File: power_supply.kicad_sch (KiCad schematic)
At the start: 10 parts, among them J1 USB4110-GF-A, U2 MIC5317-3.3YMT-TZ, U3 ACZRC5340B-G, U5 LMC7660IMX/NOPB

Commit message: Almost done. Just going to try and change something
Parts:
- removed U2: MIC5317-3.3YMT-TZ, DFN4_1X1_MCH, symbol CMPE2750:MIC5317-3.3YMT-TZ
- added U2: LP5907SNX-3.3/NOPB, DQN0004A, symbol CMPE2750:LP5907SNX-3.3_NOPB
- J1: value USB4110-GF-A -> USB4510-03-1-A; footprint USB4110-GF-A_GCT -> USB4510-03-1-A_GCT; symbol CMPE2750:USB4110-GF-A -> CMPE2750:USB4510-03-1-A
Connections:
- net GND: now also J1.B1-A12 (GND), U2.2 (GND), U2.5 (EP); no longer J1.A12-B1 (GND)
- net VBUS: now also J1.B4-A9 (VBUS), U2.3 (EN), U2.4 (VIN); no longer J1.A9-B4 (VBUS)
- net VDD: now also U2.1 (VOUT)
- no-connect marks 3 -> 5
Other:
- moved on the sheet: C1, C2, U3

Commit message: Schematic is done?
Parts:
- removed C1, C2: 1µF, LMK212G_TAY, symbol CMPE2750:LMK212B7105KGHTR
- removed U3: ACZRC5340B-G, ACZRC-G, symbol CMPE2750:ACZRC5340B-G
- added C1: 10µF, Capacitor_SMD:C_1206_3216Metric, symbol CMPE2750:CL31A106KOHNNNE
- added C2: 1µF, Capacitor_SMD:C_1206_3216Metric, symbol CMPE2750:CL31A106KOHNNNE
- added D1, D32: 5.6V~6V, Diode_SMD:D_SOD-123, symbol Device:D_Zener
- C3, C4: footprint CAP_CL31_SAM -> Capacitor_SMD:C_1206_3216Metric
- R1, R2: footprint RC0603N_YAG -> Resistor_SMD:R_0603_1608Metric
- U5: footprint M08A_TEX -> Package_SO:SOIC-8_3.9x4.9mm_P1.27mm
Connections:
- net -5V: now also D32.2 (A)
- net GND: now also C1.2, C2.2, D1.2 (A), D32.1 (K)
- net VBUS: now also C1.1, D1.1 (K)
- net VDD: now also C2.1

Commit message: Added mounting holes to the schematic, reset the annotations, updated a few footprints, and fixed some issues that were discovered on the ERC.
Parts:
- J6: renamed from J1; footprint USB4510-03-1-A_GCT -> CMPE2750:USB4510-03-1-A_GCT
- U2: footprint DQN0004A -> CMPE2750:DQN0004A
- renumbered C1 to C10, C2 to C11, C3 to C12, C4 to C13, D32 to D2, R1 to R29, R2 to R30, U5 to U3
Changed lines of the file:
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@@
+	)
+	(junction
+		(at 267.97 67.31)
+		(diameter 0)
+		(color 0 0 0 0)
 	)
 	(junction
@@
 	(wire
 		(pts
-			(xy 127 73.66) (xy 58.42 73.66)
-		)
-		(stroke
-			(width 0)
-			(type default)
-		)
-	)
-	(wire
-		(pts
 			(xy 59.69 137.16) (xy 58.42 137.16)
 		)
@@
 	(wire
 		(pts
+			(xy 58.42 73.66) (xy 127 73.66)
+		)
+		(stroke
+			(width 0)
+			(type default)
+		)
+	)
+	(wire
+		(pts
 			(xy 151.13 53.34) (xy 151.13 73.66)
 		)
@@
 	(wire
 		(pts
+			(xy 267.97 67.31) (xy 260.35 67.31)
+		)
+		(stroke
+			(width 0)
+			(type default)
+		)
+	)
+	(wire
+		(pts
 			(xy 119.38 152.4) (xy 119.38 153.67)
 		)
@@
 	(wire
 		(pts
-			(xy 271.78 67.31) (xy 260.35 67.31)
+			(xy 271.78 67.31) (xy 267.97 67.31)
 		)
 		(stroke
@@
 		(dnp no)
 		(fields_autoplaced yes)
-		(property "Reference" "C4"
+		(property "Reference" "C13"
 			(at 123.19 144.7799 90)
 			(effects
@@
 			(project ""
 				(path "/a86318a1-888d-4137-89a5-221e5a1bc171/0066a7d7-f2ad-4520-976c-e35e03c74cdf"
-					(reference "C4")
+					(reference "C13")
+					(unit 1)
+				)
+			)
+		)
+	)
+	(symbol
+		(lib_id "power:PWR_FLAG")
+		(at 267.97 67.31 0)
+		(unit 1)
+		(exclude_from_sim no)
+		(in_bom yes)
+		(on_board yes)
+		(dnp no)
+		(fields_autoplaced yes)
+		(property "Reference" "#FLG02"
+			(at 267.97 65.405 0)
+			(effects
+				(font
+					(size 1.27 1.27)
+				)
+				(hide yes)
+			)
+		)
+		(property "Value" "PWR_FLAG"
+			(at 267.97 62.23 0)
+			(effects
+				(font
+					(size 1.27 1.27)
+				)
+			)
+		)
+		(property "Footprint" ""
+			(at 267.97 67.31 0)
+			(effects
+				(font
+					(size 1.27 1.27)
+				)
+				(hide yes)
+			)
+		)
+		(property "Datasheet" "~"
+			(at 267.97 67.31 0)
+			(effects
+				(font
+					(size 1.27 1.27)
+				)
+				(hide yes)
+			)
+		)
+		(property "Description" "Special symbol for telling ERC where power comes from"
+			(at 267.97 67.31 0)
+			(effects
+				(font
+					(size 1.27 1.27)
+				)
+				(hide yes)
+			)
+		)
+		(pin "1"
+		)
+		(instances
+			(project ""
+				(path "/a86318a1-888d-4137-89a5-221e5a1bc171/0066a7d7-f2ad-4520-976c-e35e03c74cdf"
+					(reference "#FLG02")
 					(unit 1)
 				)
@@
 		(dnp no)
 		(fields_autoplaced yes)
-		(property "Reference" "U5"
+		(property "Reference" "U3"
 			(at 87.63 121.92 0)
 			(effects
@@
 					(italic yes)
 				)
+				(hide yes)
 			)
 		)
@@
 			(project ""
 				(path "/a86318a1-888d-4137-89a5-221e5a1bc171/0066a7d7-f2ad-4520-976c-e35e03c74cdf"
-					(reference "U5")
+					(reference "U3")
 					(unit 1)
 				)
@@
 		(dnp no)
 		(fields_autoplaced yes)
-		(property "Reference" "#PWR08"
+		(property "Reference" "#PWR050"
 			(at 119.38 160.02 0)
 			(effects
@@
 			(project ""
 				(path "/a86318a1-888d-4137-89a5-221e5a1bc171/0066a7d7-f2ad-4520-976c-e35e03c74cdf"
-					(reference "#PWR08")
+					(reference "#PWR050")
 					(unit 1)
 				)
@@
 		(dnp no)
 		(fields_autoplaced yes)
-		(property "Reference" "#PWR01"
+		(property "Reference" "#PWR044"
 			(at 58.42 83.82 0)
 			(effects
@@
 			(project ""
 				(path "/a86318a1-888d-4137-89a5-221e5a1bc171/0066a7d7-f2ad-4520-976c-e35e03c74cdf"
-					(reference "#PWR01")
+					(reference "#PWR044")
 					(unit 1)
 				)
@@
 		(dnp no)
 		(fields_autoplaced yes)
-		(property "Reference" "#PWR03"
+		(property "Reference" "#PWR045"
 			(at 198.12 88.9 0)
 			(effects
@@
 			(project ""
 				(path "/a86318a1-888d-4137-89a5-221e5a1bc171/0066a7d7-f2ad-4520-976c-e35e03c74cdf"
-					(reference "#PWR03")
+					(reference "#PWR045")
 					(unit 1)
 				)
@@
 		(dnp no)
 		(fields_autoplaced yes)
-		(property "Reference" "C2"
+		(property "Reference" "C11"
 			(at 264.16 77.4699 90)
 			(effects
@@
 			(project "CMPE2750"
 				(path "/a86318a1-888d-4137-89a5-221e5a1bc171/0066a7d7-f2ad-4520-976c-e35e03c74cdf"
-					(reference "C2")
+					(reference "C11")
 					(unit 1)
 				)
@@
 		(dnp no)
 		(fields_autoplaced yes)
-		(property "Reference" "#PWR07"
+		(property "Reference" "#PWR049"
 			(at 58.42 149.86 0)
 			(effects
@@
 			(project ""
 				(path "/a86318a1-888d-4137-89a5-221e5a1bc171/0066a7d7-f2ad-4520-976c-e35e03c74cdf"
-					(reference "#PWR07")
+					(reference "#PWR049")
 					(unit 1)
 				)
@@
 		(dnp no)
 		(fields_autoplaced yes)
-		(property "Reference" "#PWR05"
+		(property "Reference" "#PWR043"
 			(at 209.55 64.77 0)
 			(effects
@@
 			(project ""
 				(path "/a86318a1-888d-4137-89a5-221e5a1bc171/0066a7d7-f2ad-4520-976c-e35e03c74cdf"
-					(reference "#PWR05")
+					(reference "#PWR043")
 					(unit 1)
 				)
@@
 		(dnp no)
 		(fields_autoplaced yes)
-		(property "Reference" "J1"
+		(property "Reference" "J6"
 			(at 104.14 35.56 0)
 			(effects
@@
 			)
 		)
-		(property "Footprint" "USB4510-03-1-A_GCT"
+		(property "Footprint" "CMPE2750:USB4510-03-1-A_GCT"
 			(at 83.82 45.72 0)
 			(effects
@@
 			(project ""
 				(path "/a86318a1-888d-4137-89a5-221e5a1bc171/0066a7d7-f2ad-4520-976c-e35e03c74cdf"
-					(reference "J1")
+					(reference "J6")
 					(unit 1)
 				)
@@
 		(on_board yes)
 		(dnp no)
-		(property "Reference" "R2"
+		(property "Reference" "R30"
 			(at 137.16 49.53 0)
 			(effects
@@
 			(project ""
 				(path "/a86318a1-888d-4137-89a5-221e5a1bc171/0066a7d7-f2ad-4520-976c-e35e03c74cdf"
-					(reference "R2")
+					(reference "R30")
 					(unit 1)
 				)
@@
 		(dnp no)
 		(fields_autoplaced yes)
-		(property "Reference" "#PWR010"
+		(property "Reference" "#PWR048"
 			(at 124.46 140.97 0)
 			(effects
@@
 			(project ""
 				(path "/a86318a1-888d-4137-89a5-221e5a1bc171/0066a7d7-f2ad-4520-976c-e35e03c74cdf"
-					(reference "#PWR010")
+					(reference "#PWR048")
 					(unit 1)
 				)
@@
 		(dnp no)
 		(fields_autoplaced yes)
-		(property "Reference" "#PWR06"
+		(property "Reference" "#PWR046"
 			(at 250.19 102.87 0)
 			(effects
@@
 			(project ""
 				(path "/a86318a1-888d-4137-89a5-221e5a1bc171/0066a7d7-f2ad-4520-976c-e35e03c74cdf"
-					(reference "#PWR06")
+					(reference "#PWR046")
 					(unit 1)
 				)
@@
 		(dnp no)
 		(fields_autoplaced yes)
-		(property "Reference" "#PWR09"
+		(property "Reference" "#PWR047"
 			(at 120.65 132.08 0)
 			(effects
@@
 			(project ""
 				(path "/a86318a1-888d-4137-89a5-221e5a1bc171/0066a7d7-f2ad-4520-976c-e35e03c74cdf"
-					(reference "#PWR09")
+					(reference "#PWR047")
 					(unit 1)
 				)
@@
 		(dnp no)
 		(fields_autoplaced yes)
-		(property "Reference" "#PWR04"
+		(property "Reference" "#PWR042"
 			(at 138.43 31.75 0)
 			(effects
@@
 			(project ""
 				(path "/a86318a1-888d-4137-89a5-221e5a1bc171/0066a7d7-f2ad-4520-976c-e35e03c74cdf"
-					(reference "#PWR04")
+					(reference "#PWR042")
 					(unit 1)
 				)
@@
 		(on_board yes)
 		(dnp no)
-		(property "Reference" "R1"
+		(property "Reference" "R29"
 			(at 71.12 46.99 0)
 			(effects
@@
 			(project ""
 				(path "/a86318a1-888d-4137-89a5-221e5a1bc171/0066a7d7-f2ad-4520-976c-e35e03c74cdf"
-					(reference "R1")
+					(reference "R29")
 					(unit 1)
 				)
@@
 		(dnp no)
 		(fields_autoplaced yes)
-		(property "Reference" "C1"
+		(property "Reference" "C10"
 			(at 205.74 74.9299 90)
 			(effects
@@
 			(project "CMPE2750"
 				(path "/a86318a1-888d-4137-89a5-221e5a1bc171/0066a7d7-f2ad-4520-976c-e35e03c74cdf"
-					(reference "C1")
+					(reference "C10")
 					(unit 1)
 				)
@@
 			)
 		)
-		(property "Footprint" "DQN0004A"
+		(property "Footprint" "CMPE2750:DQN0004A"
 			(at 228.6 77.47 0)
 			(effects
@@
 		(on_board yes)
 		(dnp no)
-		(property "Reference" "C3"
+		(property "Reference" "C12"
 			(at 46.99 140.9701 90)
 			(effects
@@
 			(project ""
 				(path "/a86318a1-888d-4137-89a5-221e5a1bc171/0066a7d7-f2ad-4520-976c-e35e03c74cdf"
-					(reference "C3")
+					(reference "C12")
 					(unit 1)
 				)
@@
 		(on_board yes)
 		(dnp no)
-		(property "Reference" "D32"
+		(property "Reference" "D2"
 			(at 143.002 146.812 90)
 			(effects
@@
 			(project "CMPE2750"
 				(path "/a86318a1-888d-4137-89a5-221e5a1bc171/0066a7d7-f2ad-4520-976c-e35e03c74cdf"
-					(reference "D32")
+					(reference "D2")
 					(unit 1)
 				)

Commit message: Added a ferrite bead and removed a decoupling cap from another ferrite bead
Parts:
- renumbered C11 to C10, C12 to C11, C13 to C12, C10 to C9
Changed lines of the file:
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@@
 		(dnp no)
 		(fields_autoplaced yes)
-		(property "Reference" "C13"
+		(property "Reference" "C12"
 			(at 123.19 144.7799 90)
 			(effects
@@
 			(project ""
 				(path "/a86318a1-888d-4137-89a5-221e5a1bc171/0066a7d7-f2ad-4520-976c-e35e03c74cdf"
-					(reference "C13")
+					(reference "C12")
 					(unit 1)
 				)
@@
 		(dnp no)
 		(fields_autoplaced yes)
-		(property "Reference" "#PWR050"
+		(property "Reference" "#PWR049"
 			(at 119.38 160.02 0)
 			(effects
@@
 			(project ""
 				(path "/a86318a1-888d-4137-89a5-221e5a1bc171/0066a7d7-f2ad-4520-976c-e35e03c74cdf"
-					(reference "#PWR050")
+					(reference "#PWR049")
 					(unit 1)
 				)
@@
 		(dnp no)
 		(fields_autoplaced yes)
-		(property "Reference" "#PWR044"
+		(property "Reference" "#PWR043"
 			(at 58.42 83.82 0)
 			(effects
@@
 			(project ""
 				(path "/a86318a1-888d-4137-89a5-221e5a1bc171/0066a7d7-f2ad-4520-976c-e35e03c74cdf"
-					(reference "#PWR044")
+					(reference "#PWR043")
 					(unit 1)
 				)
@@
 		(dnp no)
 		(fields_autoplaced yes)
-		(property "Reference" "#PWR045"
+		(property "Reference" "#PWR044"
 			(at 198.12 88.9 0)
 			(effects
@@
 			(project ""
 				(path "/a86318a1-888d-4137-89a5-221e5a1bc171/0066a7d7-f2ad-4520-976c-e35e03c74cdf"
-					(reference "#PWR045")
+					(reference "#PWR044")
 					(unit 1)
 				)
@@
 		(dnp no)
 		(fields_autoplaced yes)
-		(property "Reference" "C11"
+		(property "Reference" "C10"
 			(at 264.16 77.4699 90)
 			(effects
@@
 			(project "CMPE2750"
 				(path "/a86318a1-888d-4137-89a5-221e5a1bc171/0066a7d7-f2ad-4520-976c-e35e03c74cdf"
-					(reference "C11")
+					(reference "C10")
 					(unit 1)
 				)
@@
 		(dnp no)
 		(fields_autoplaced yes)
-		(property "Reference" "#PWR049"
+		(property "Reference" "#PWR048"
 			(at 58.42 149.86 0)
 			(effects
@@
 			(project ""
 				(path "/a86318a1-888d-4137-89a5-221e5a1bc171/0066a7d7-f2ad-4520-976c-e35e03c74cdf"
-					(reference "#PWR049")
+					(reference "#PWR048")
 					(unit 1)
 				)
@@
 		(dnp no)
 		(fields_autoplaced yes)
-		(property "Reference" "#PWR043"
+		(property "Reference" "#PWR042"
 			(at 209.55 64.77 0)
 			(effects
@@
 			(project ""
 				(path "/a86318a1-888d-4137-89a5-221e5a1bc171/0066a7d7-f2ad-4520-976c-e35e03c74cdf"
-					(reference "#PWR043")
+					(reference "#PWR042")
 					(unit 1)
 				)
@@
 		(dnp no)
 		(fields_autoplaced yes)
-		(property "Reference" "#PWR048"
+		(property "Reference" "#PWR047"
 			(at 124.46 140.97 0)
 			(effects
@@
 			(project ""
 				(path "/a86318a1-888d-4137-89a5-221e5a1bc171/0066a7d7-f2ad-4520-976c-e35e03c74cdf"
-					(reference "#PWR048")
+					(reference "#PWR047")
 					(unit 1)
 				)
@@
 		(dnp no)
 		(fields_autoplaced yes)
-		(property "Reference" "#PWR046"
+		(property "Reference" "#PWR045"
 			(at 250.19 102.87 0)
 			(effects
@@
 			(project ""
 				(path "/a86318a1-888d-4137-89a5-221e5a1bc171/0066a7d7-f2ad-4520-976c-e35e03c74cdf"
-					(reference "#PWR046")
+					(reference "#PWR045")
 					(unit 1)
 				)
@@
 		(dnp no)
 		(fields_autoplaced yes)
-		(property "Reference" "#PWR047"
+		(property "Reference" "#PWR046"
 			(at 120.65 132.08 0)
 			(effects
@@
 			(project ""
 				(path "/a86318a1-888d-4137-89a5-221e5a1bc171/0066a7d7-f2ad-4520-976c-e35e03c74cdf"
-					(reference "#PWR047")
+					(reference "#PWR046")
 					(unit 1)
 				)
@@
 		(dnp no)
 		(fields_autoplaced yes)
-		(property "Reference" "#PWR042"
+		(property "Reference" "#PWR041"
 			(at 138.43 31.75 0)
 			(effects
@@
 			(project ""
 				(path "/a86318a1-888d-4137-89a5-221e5a1bc171/0066a7d7-f2ad-4520-976c-e35e03c74cdf"
-					(reference "#PWR042")
+					(reference "#PWR041")
 					(unit 1)
 				)
@@
 		(dnp no)
 		(fields_autoplaced yes)
-		(property "Reference" "C10"
+		(property "Reference" "C9"
 			(at 205.74 74.9299 90)
 			(effects
@@
 			(project "CMPE2750"
 				(path "/a86318a1-888d-4137-89a5-221e5a1bc171/0066a7d7-f2ad-4520-976c-e35e03c74cdf"
-					(reference "C10")
+					(reference "C9")
 					(unit 1)
 				)
@@
 		(on_board yes)
 		(dnp no)
-		(property "Reference" "C12"
+		(property "Reference" "C11"
 			(at 46.99 140.9701 90)
 			(effects
@@
 			(project ""
 				(path "/a86318a1-888d-4137-89a5-221e5a1bc171/0066a7d7-f2ad-4520-976c-e35e03c74cdf"
-					(reference "C12")
-					(unit 1)
-				)
+					(reference "C11")
+					(unit 1)
+				)

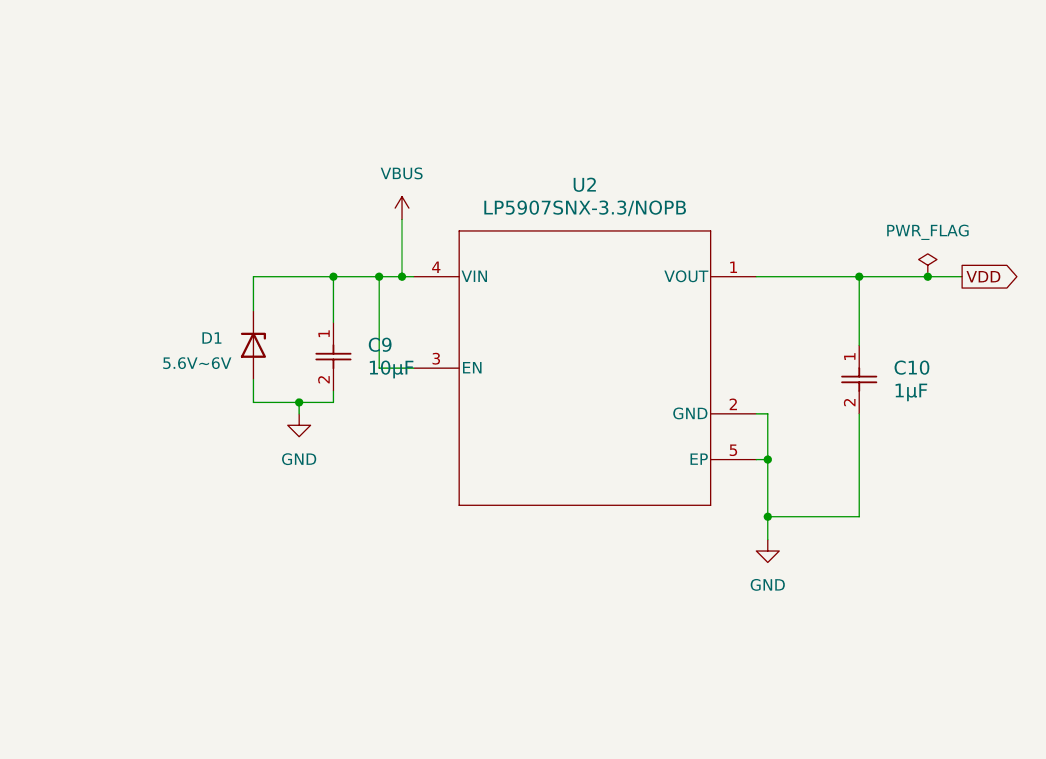
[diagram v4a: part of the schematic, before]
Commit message: Component placing partly done. Saving before overwriting the pcb with the templating script output
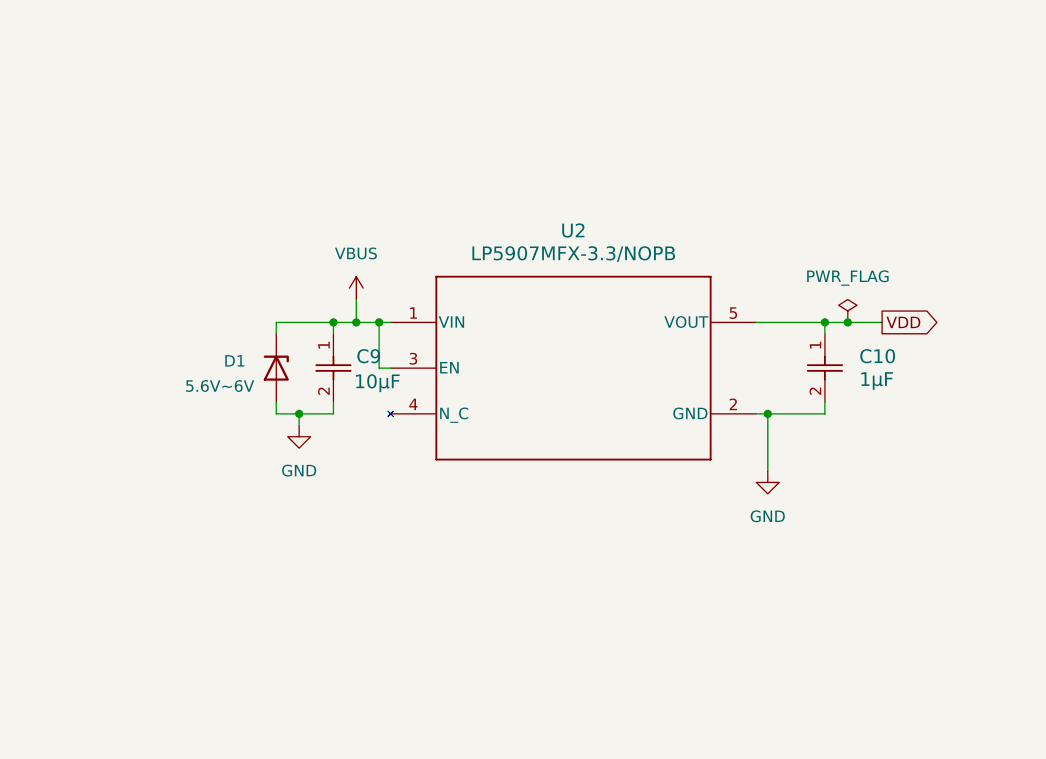
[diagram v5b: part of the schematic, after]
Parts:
- U2: value LP5907SNX-3.3/NOPB -> LP5907MFX-3.3/NOPB; footprint CMPE2750:DQN0004A -> DBV0005A_N; symbol CMPE2750:LP5907SNX-3.3_NOPB -> CMPE2750:LP5907MFX-3.3_NOPB
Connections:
- net GND: no longer U2.5 (EP)
- net VBUS: now also U2.1 (VIN); no longer U2.4 (VIN)
- net VDD: now also U2.5 (VOUT); no longer U2.1 (VOUT)
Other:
- moved on the sheet: C10, C9, D1

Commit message: pcb almost done, just need to do the final copper fill
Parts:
- added C31: 4.7nF 1kV, Capacitor_SMD:C_1206_3216Metric, symbol Device:C
- added R14: 1MΩ, Resistor_SMD:R_2512_6332Metric, symbol Device:R_US
- J6: value USB4510-03-1-A -> TYPE-C-31-M-12; footprint CMPE2750:USB4510-03-1-A_GCT -> Connector_USB:USB_C_Receptacle_HRO_TYPE-C-31-M-12; symbol CMPE2750:USB4510-03-1-A -> Connector:USB_C_Receptacle_USB2.0_16P
- U2: footprint DBV0005A_N -> CMPE2750:DBV0005A_N
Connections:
- net GND: now also J6.A1 (GND), J6.A12 (GND), J6.B1 (GND), J6.B12 (GND), R29.2, C31.2, R14.2; no longer J6.A1-B12 (GND), J6.B1-A12 (GND), R29.1
- net VBUS: now also J6.A4 (VBUS), J6.A9 (VBUS), J6.B4 (VBUS), J6.B9 (VBUS); no longer J6.A4-B9 (VBUS), J6.B4-A9 (VBUS)
- net at J6.A5 (CC1): now also R29.1; no longer R29.2
- new net: C31.1, J6.S1 (SHIELD), R14.1
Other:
- moved on the sheet: R29, R30
